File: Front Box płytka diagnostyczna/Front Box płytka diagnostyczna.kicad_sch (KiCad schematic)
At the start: 7 parts, among them J2 APPS, J3 EBS, J4 Karta, J5 Conn_01x02, J6 Wolne, J7 Telemetria

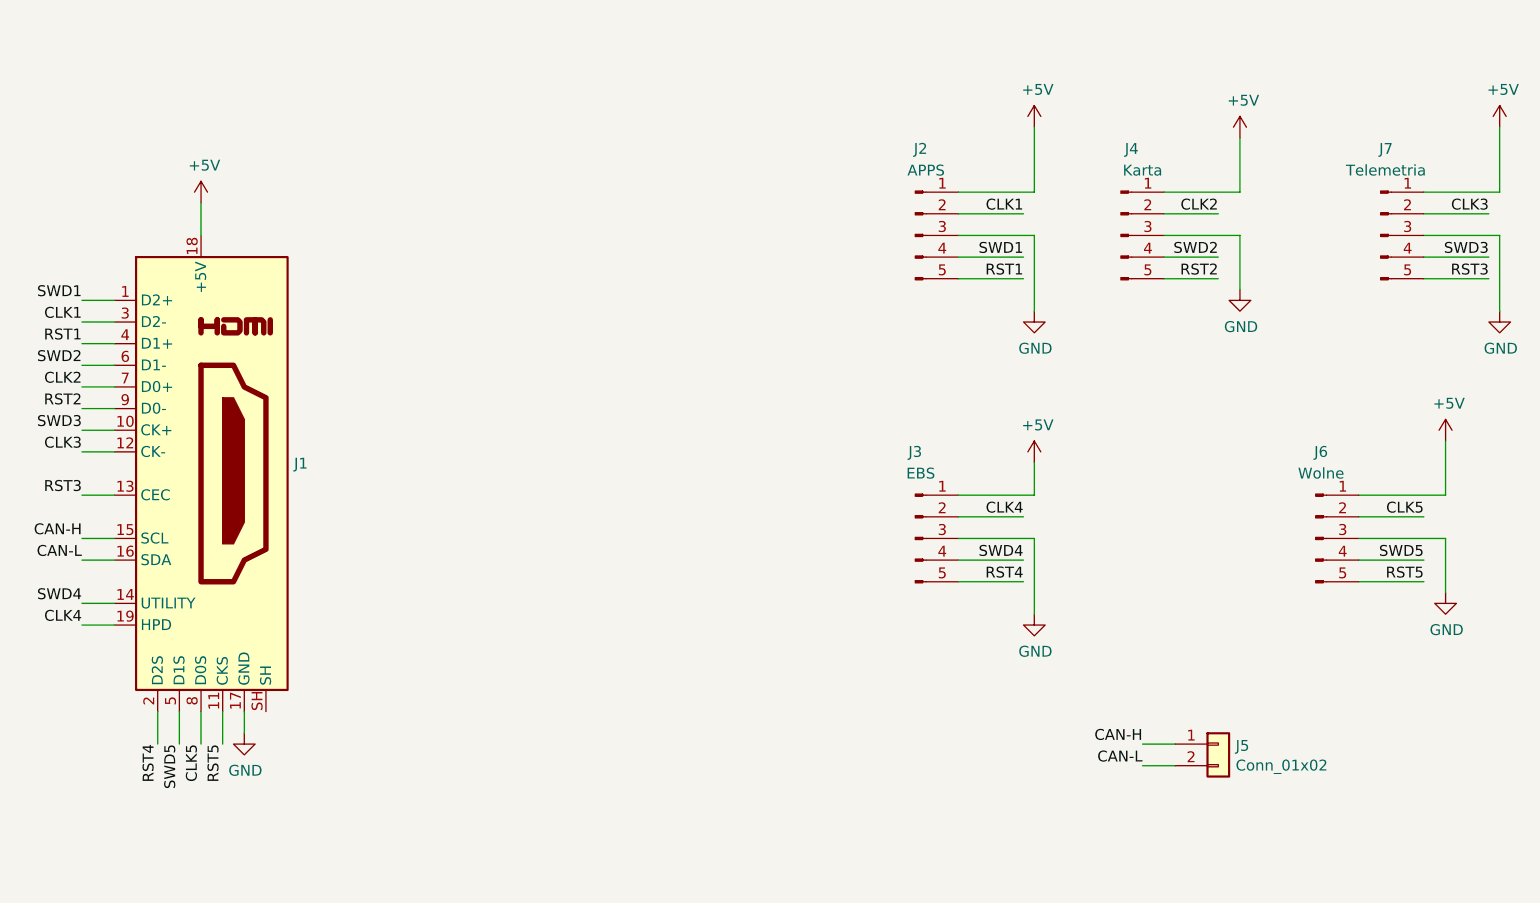
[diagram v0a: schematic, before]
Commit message: New silkscreen and connectors for diagnostic board
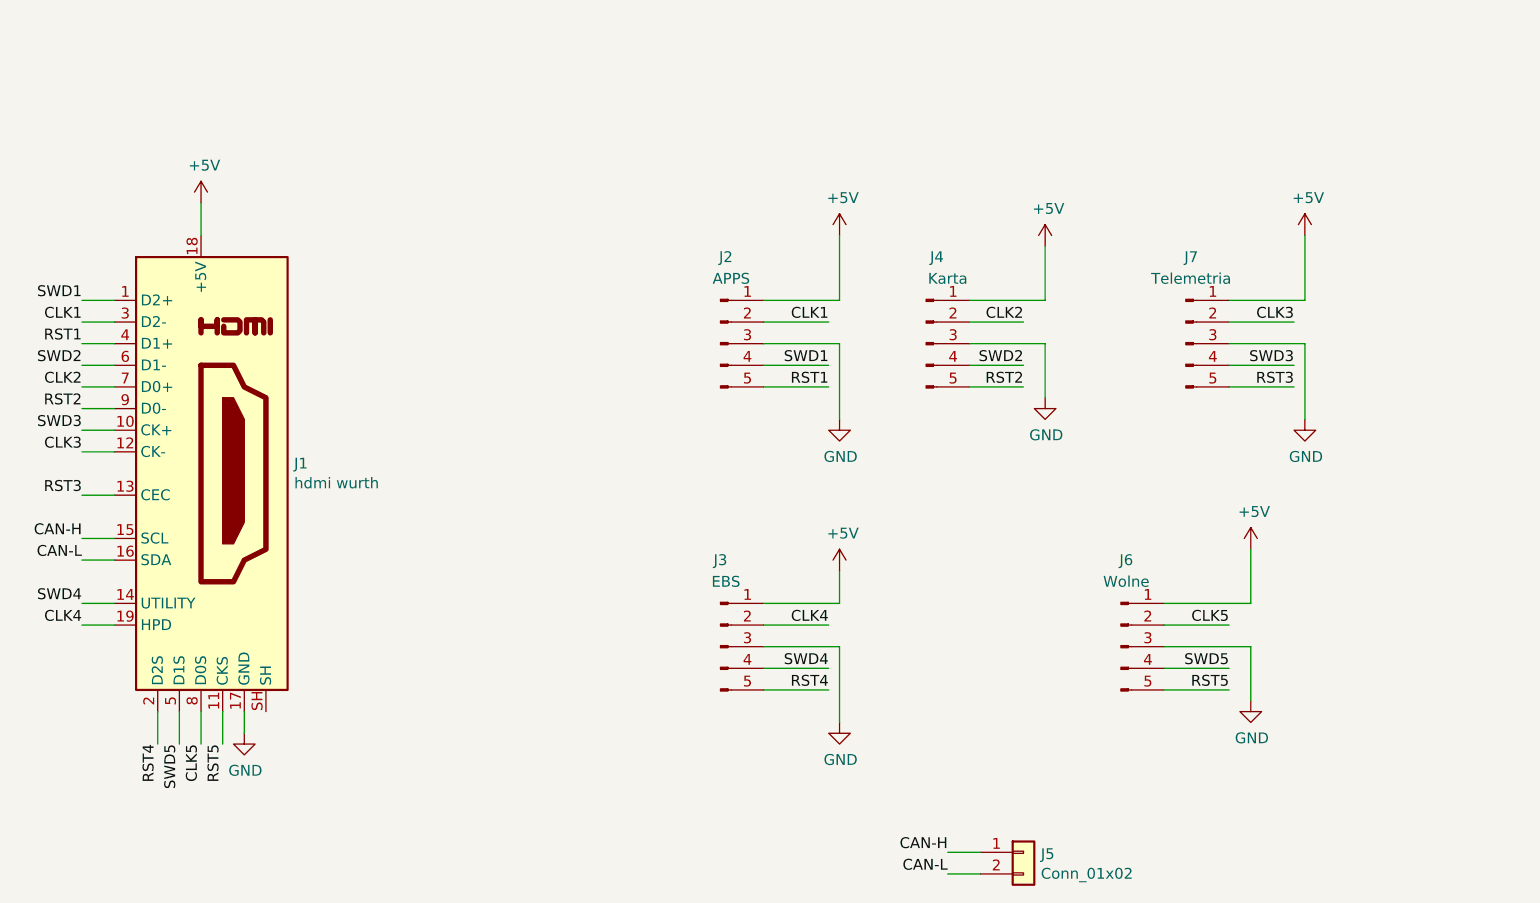
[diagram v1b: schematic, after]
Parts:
- J1: value (none) -> hdmi wurth; footprint (none) -> footprints:685119134923
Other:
- moved on the sheet: J2, J3, J4, J5, J6, J7

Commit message: PCB prepared for gerber generation
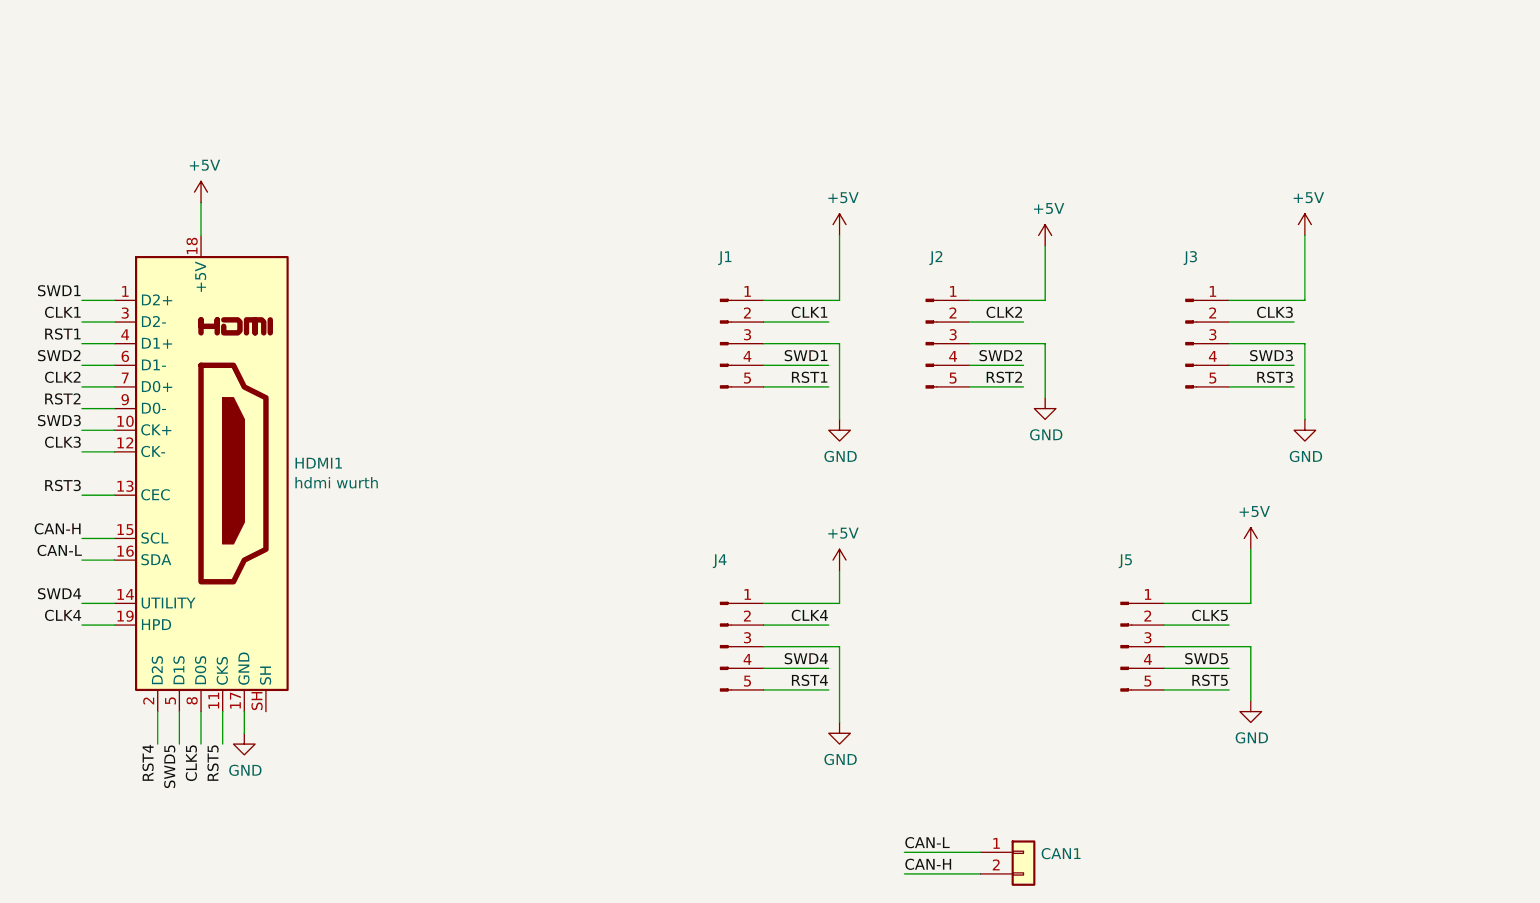
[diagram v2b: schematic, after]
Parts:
- CAN1: renamed from J5; value Conn_01x02 -> (none)
- J1: renamed from J2; value APPS -> (none); footprint Connector_PinHeader_2.54mm:PinHeader_1x05_P2.54mm_Vertical -> (none)
- J2: renamed from J4; value Karta -> (none); footprint Connector_PinHeader_2.54mm:PinHeader_1x05_P2.54mm_Vertical -> (none)
- J3: renamed from J7; value Telemetria -> (none); footprint Connector_PinHeader_2.54mm:PinHeader_1x05_P2.54mm_Vertical -> (none)
- J4: renamed from J3; value EBS -> (none); footprint Connector_PinHeader_2.54mm:PinHeader_1x05_P2.54mm_Vertical -> (none)
- J5: renamed from J6; value Wolne -> (none); footprint Connector_PinHeader_2.54mm:PinHeader_1x05_P2.54mm_Vertical -> (none)
- renumbered J1 to HDMI1
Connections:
- net CAN-H: now also CAN1.2 (Pin_2); no longer CAN1.1 (Pin_1)
- net CAN-L: now also CAN1.1 (Pin_1); no longer CAN1.2 (Pin_2)
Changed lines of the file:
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@@
+    (stroke (width 0) (type default) (color 0 0 0 0))
+  )
+  (wire (pts (xy 158.75 134.62) (xy 167.64 134.62))
     (stroke (width 0) (type default) (color 0 0 0 0))
   )
@@
     (stroke (width 0) (type default) (color 0 0 0 0))
   )
-  (wire (pts (xy 163.83 134.62) (xy 167.64 134.62))
-    (stroke (width 0) (type default) (color 0 0 0 0))
-  )
   (wire (pts (xy 62.23 107.95) (xy 66.04 107.95))
     (stroke (width 0) (type default) (color 0 0 0 0))
   )
-  (wire (pts (xy 163.83 137.16) (xy 167.64 137.16))
-    (stroke (width 0) (type default) (color 0 0 0 0))
-  )
   (wire (pts (xy 204.47 80.01) (xy 196.85 80.01))
     (stroke (width 0) (type default) (color 0 0 0 0))
@@
     (stroke (width 0) (type default) (color 0 0 0 0))
   )
+  (wire (pts (xy 158.75 137.16) (xy 167.64 137.16))
+    (stroke (width 0) (type default) (color 0 0 0 0))
+  )
   (wire (pts (xy 149.86 113.03) (xy 142.24 113.03))
     (stroke (width 0) (type default) (color 0 0 0 0))
@@
     (effects (font (size 1.27 1.27)) (justify right bottom))
   )
-  (label "CAN-L" (at 163.83 137.16 180)
-    (effects (font (size 1.27 1.27)) (justify right bottom))
+  (label "CAN-L" (at 158.75 134.62 0)
+    (effects (font (size 1.27 1.27)) (justify left bottom))
   )
   (label "SWD5" (at 196.85 113.03 180)
@@
     (effects (font (size 1.27 1.27)) (justify right bottom))
   )
-  (label "CAN-H" (at 163.83 134.62 180)
-    (effects (font (size 1.27 1.27)) (justify right bottom))
+  (label "CAN-H" (at 158.75 137.16 0)
+    (effects (font (size 1.27 1.27)) (justify left bottom))
   )
   (label "SWD2" (at 172.72 77.47 180)
@@
   (symbol (lib_id "Connector:HDMI_A") (at 76.2 90.17 0) (unit 1)
     (in_bom yes) (on_board yes)
-    (property "Reference" "J1" (id 0) (at 87.122 89.0016 0)
+    (property "Reference" "HDMI1" (id 0) (at 87.122 89.0016 0)
       (effects (font (size 1.27 1.27)) (justify left))
     )
@@
   (symbol (lib_id "Connector:Conn_01x05_Male") (at 184.15 110.49 0) (unit 1)
     (in_bom yes) (on_board yes) (fields_autoplaced)
-    (property "Reference" "J6" (id 0) (at 184.785 100.33 0))
-    (property "Value" "Wolne" (id 1) (at 184.785 102.87 0))
-    (property "Footprint" "Connector_PinHeader_2.54mm:PinHeader_1x05_P2.54mm_Vertical" (id 2) (at 184.15 110.49 0)
+    (property "Reference" "J5" (id 0) (at 184.785 100.33 0))
+    (property "Value" "" (id 1) (at 184.785 102.87 0))
+    (property "Footprint" "" (id 2) (at 184.15 110.49 0)
       (effects (font (size 1.27 1.27)) hide)
     )
@@
   (symbol (lib_id "Connector:Conn_01x05_Male") (at 137.16 110.49 0) (unit 1)
     (in_bom yes) (on_board yes)
-    (property "Reference" "J3" (id 0) (at 137.16 100.33 0))
-    (property "Value" "EBS" (id 1) (at 137.795 102.87 0))
-    (property "Footprint" "Connector_PinHeader_2.54mm:PinHeader_1x05_P2.54mm_Vertical" (id 2) (at 137.16 110.49 0)
+    (property "Reference" "J4" (id 0) (at 137.16 100.33 0))
+    (property "Value" "" (id 1) (at 137.795 102.87 0))
+    (property "Footprint" "" (id 2) (at 137.16 110.49 0)
       (effects (font (size 1.27 1.27)) hide)
     )
@@
   (symbol (lib_id "Connector_Generic:Conn_01x02") (at 172.72 134.62 0) (unit 1)
     (in_bom yes) (on_board yes)
-    (property "Reference" "J5" (id 0) (at 174.752 134.8232 0)
+    (property "Reference" "CAN1" (id 0) (at 174.752 134.8232 0)
       (effects (font (size 1.27 1.27)) (justify left))
     )
-    (property "Value" "Conn_01x02" (id 1) (at 174.752 137.1346 0)
+    (property "Value" "" (id 1) (at 174.752 137.1346 0)
       (effects (font (size 1.27 1.27)) (justify left))
     )
@@
   (symbol (lib_id "Connector:Conn_01x05_Male") (at 161.29 74.93 0) (unit 1)
     (in_bom yes) (on_board yes)
-    (property "Reference" "J4" (id 0) (at 162.56 64.77 0))
-    (property "Value" "Karta " (id 1) (at 163.83 67.31 0))
-    (property "Footprint" "Connector_PinHeader_2.54mm:PinHeader_1x05_P2.54mm_Vertical" (id 2) (at 161.29 74.93 0)
+    (property "Reference" "J2" (id 0) (at 162.56 64.77 0))
+    (property "Value" "" (id 1) (at 163.83 67.31 0))
+    (property "Footprint" "" (id 2) (at 161.29 74.93 0)
       (effects (font (size 1.27 1.27)) hide)
     )
@@
   (symbol (lib_id "Connector:Conn_01x05_Male") (at 191.77 74.93 0) (unit 1)
     (in_bom yes) (on_board yes) (fields_autoplaced)
-    (property "Reference" "J7" (id 0) (at 192.405 64.77 0))
-    (property "Value" "Telemetria" (id 1) (at 192.405 67.31 0))
-    (property "Footprint" "Connector_PinHeader_2.54mm:PinHeader_1x05_P2.54mm_Vertical" (id 2) (at 191.77 74.93 0)
+    (property "Reference" "J3" (id 0) (at 192.405 64.77 0))
+    (property "Value" "" (id 1) (at 192.405 67.31 0))
+    (property "Footprint" "" (id 2) (at 191.77 74.93 0)
       (effects (font (size 1.27 1.27)) hide)
     )
@@
   (symbol (lib_id "Connector:Conn_01x05_Male") (at 137.16 74.93 0) (unit 1)
     (in_bom yes) (on_board yes)
-    (property "Reference" "J2" (id 0) (at 137.795 64.77 0))
-    (property "Value" "APPS" (id 1) (at 138.43 67.31 0))
-    (property "Footprint" "Connector_PinHeader_2.54mm:PinHeader_1x05_P2.54mm_Vertical" (id 2) (at 137.16 74.93 0)
+    (property "Reference" "J1" (id 0) (at 137.795 64.77 0))
+    (property "Value" "" (id 1) (at 138.43 67.31 0))
+    (property "Footprint" "" (id 2) (at 137.16 74.93 0)
       (effects (font (size 1.27 1.27)) hide)
     )
@@
       (reference "#PWR0112") (unit 1) (value "+5V") (footprint "")
     )
+    (path "/356199c8-c0f7-4995-bef0-53ad752a30c5"
+      (reference "CAN1") (unit 1) (value "Male header 2.54mm") (footprint "Connector_PinHeader_2.54mm:PinHeader_1x02_P2.54mm_Vertical")
+    )
     (path "/08ac4c42-16f0-4513-b91e-bf0b3a111257"
-      (reference "J1") (unit 1) (value "hdmi wurth") (footprint "footprints:685119134923")
+      (reference "HDMI1") (unit 1) (value "hdmi wurth") (footprint "footprints:685119134923")
     )
     (path "/e8e598ff-c991-433d-8dd6-c9fce2fe1eaa"
-      (reference "J2") (unit 1) (value "APPS") (footprint "Connector_PinHeader_2.54mm:PinHeader_1x05_P2.54mm_Vertical")
+      (reference "J1") (unit 1) (value "APPS") (footprint "Connector_PinHeader_2.54mm:PinHeader_1x05_P2.54mm_Vertical")
+    )
+    (path "/3d2a15cb-c492-4d9a-b1dd-7d5f099d2d31"
+      (reference "J2") (unit 1) (value "Karta") (footprint "Connector_PinHeader_2.54mm:PinHeader_1x05_P2.54mm_Vertical")
+    )
+    (path "/41ab46ed-40f5-461d-81aa-1f02dc069a49"
+      (reference "J3") (unit 1) (value "Telemetria") (footprint "Connector_PinHeader_2.54mm:PinHeader_1x05_P2.54mm_Vertical")
     )
     (path "/1020b588-7eb0-4b70-bbff-c77a867c3142"
-      (reference "J3") (unit 1) (value "EBS") (footprint "Connector_PinHeader_2.54mm:PinHeader_1x05_P2.54mm_Vertical")
-    )
-    (path "/3d2a15cb-c492-4d9a-b1dd-7d5f099d2d31"
-      (reference "J4") (unit 1) (value "Karta ") (footprint "Connector_PinHeader_2.54mm:PinHeader_1x05_P2.54mm_Vertical")
-    )
-    (path "/356199c8-c0f7-4995-bef0-53ad752a30c5"
-      (reference "J5") (unit 1) (value "Conn_01x02") (footprint "Connector_PinHeader_2.54mm:PinHeader_1x02_P2.54mm_Vertical")
+      (reference "J4") (unit 1) (value "EBS") (footprint "Connector_PinHeader_2.54mm:PinHeader_1x05_P2.54mm_Vertical")
     )
     (path "/0df798c0-963e-4340-a737-18e50763521e"
-      (reference "J6") (unit 1) (value "Wolne") (footprint "Connector_PinHeader_2.54mm:PinHeader_1x05_P2.54mm_Vertical")
-    )
-    (path "/41ab46ed-40f5-461d-81aa-1f02dc069a49"
-      (reference "J7") (unit 1) (value "Telemetria") (footprint "Connector_PinHeader_2.54mm:PinHeader_1x05_P2.54mm_Vertical")
-    )
-  )
+      (reference "J5") (unit 1) (value "Wolne") (footprint "Connector_PinHeader_2.54mm:PinHeader_1x05_P2.54mm_Vertical")
+    )
+  )
